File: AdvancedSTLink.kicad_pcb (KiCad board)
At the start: 2 copper layers, 61 x 19 mm, 50 parts, among them J1 USB_C_Receptacle, J2 Conn_02x03_Odd_Even, J3 Conn_01x06, SW1 SW_SPDT, U1 STM32F205RETx, U2 XC6206P332MR, U3 USBLC6-2P6, U4 MP2359, U5 USBLC6-2P6, U6 USBLC6-2P6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

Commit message: fabrication version
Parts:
- J3: value Conn_01x06 -> Conn_01x06_MountingPin
- moved J3 0.11 mm to (206.9, 106.4)
- moved D4 0.08 mm to (190.9, 113.0)
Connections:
- J3 pad MP: (no net) -> GND
- R1 pad 2: TCK1 -> RST1
- R6 pad 2: TCK2 -> RST2
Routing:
- net RST2: track 0.00 -> 41.2 mm, vias 0 -> 4
- net RST1: track 0.00 -> 37.2 mm, vias 0 -> 4
- net TCK1: track 59.6 -> 51.0 mm
- net TCK2: track 49.0 -> 41.8 mm, vias 4 -> 2
- net Net-(R2-Pad2): track 23.6 -> 21.7 mm, vias 2 -> 0
- net +3V3: track 111.9 -> 111.0 mm
- net GND: track 7.60 -> 7.08 mm, vias 62 -> 81
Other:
- board text added: "J8Link"
- board text removed: "STLink"

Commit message: Rev 2
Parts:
- removed R10, R11, R12, R13, R18, R6: 220, Resistor_SMD:R_0603_1608Metric
- added D6: LED_Blue, LED_SMD:LED_0603_1608Metric_Pad1.05x0.95mm_HandSolder, F.Cu at (161.3, 136.5)
- added D7: SS34, lc:SMA(DO-214AC)_S1, F.Cu at (154.1, 137.3)
- added J4: Conn_02x03_Odd_Even, Connector_PinHeader_1.27mm:PinHeader_2x03_P1.27mm_Vertical, F.Cu at (165.1, 128.5)
- added RN1: 220×4, lc:0402_RX4, F.Cu at (170.3, 128.4)
- added RN2: 220×4, lc:0402_RX4, F.Cu at (165.3, 134.3)
- C1, C2: value 10pF -> 12pF; footprint Capacitor_SMD:C_0603_1608Metric -> Capacitor_SMD:C_0402_1005Metric
- C10, C11, C13, C14, C3, C4, C5, C7, C8, C9: footprint Capacitor_SMD:C_0603_1608Metric -> Capacitor_SMD:C_0402_1005Metric
- D3: value B230A -> SS34; footprint Diode_SMD:D_SMA -> lc:SMA(DO-214AC)_S1
- D4: footprint Diode_SMD:D_SOD-123 -> lc:SOD-123
- J3: value Conn_01x06_MountingPin -> Conn_01x06
- R1: value 220 -> 39k; footprint Resistor_SMD:R_0603_1608Metric -> Resistor_SMD:R_0402_1005Metric
- R14, R15, R17, R2, R4, R5, R7, R8: footprint Resistor_SMD:R_0603_1608Metric -> Resistor_SMD:R_0402_1005Metric
- R16: value 1.5k -> 1.8k; footprint Resistor_SMD:R_0603_1608Metric -> Resistor_SMD:R_0402_1005Metric
- R9: value 330k -> 2.2k; footprint Resistor_SMD:R_0603_1608Metric -> Resistor_SMD:R_0402_1005Metric
- U1: moved to B.Cu
- U2: footprint Package_TO_SOT_SMD:SOT-23 -> lc:SOT-23-3L
- U4: footprint Package_TO_SOT_SMD:SOT-23-6 -> lc:SOT-23-6
- Y1: value DXS321G 8MHz -> NX3225GA-12MHz
- moved J3 56.3 mm to (156.5, 131.4), turned to 0 degrees
- moved R1 53.0 mm to (160.5, 138.8), turned to 0 degrees
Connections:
- C6 pad 1: VBUS -> Net-(C6-Pad1)
- J3 pad MP: GND -> (no net)
- R1 pad 2: RST1 -> Net-(D6-Pad2)
- R9 pad 1: VBUS -> +3V3
- SW1 pad 1: GND -> Net-(R9-Pad2)
- SW1 pad 2: Net-(R9-Pad2) -> Net-(D6-Pad2)
- SW1 pad 3: Net-(SW1-Pad3) -> GND
- U4 pad 4: Net-(R9-Pad2) -> Net-(R1-Pad1)
- U4 pad 5: VBUS -> Net-(C6-Pad1)
- U5 pad 4: Net-(R12-Pad2) -> T_SWO_I
- U5 pad 6: Net-(R1-Pad1) -> T_NRST_I
- U6 pad 4: Net-(R13-Pad2) -> T_SWDIO_I
- U6 pad 6: Net-(R10-Pad1) -> T_SWCLK_I
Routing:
- net +3V3: track 111.0 -> 0.00 mm, vias 10 -> 0
- net VBUS: track 57.8 -> 0.00 mm
- net TCK1: track 51.0 -> 0.00 mm
- net V_OUT_3.3: track 47.7 -> 0.00 mm, vias 4 -> 0
- net TDO: track 43.0 -> 0.00 mm, vias 2 -> 0
- net TCK2: track 41.8 -> 0.00 mm, vias 2 -> 0
- net RST2: track 41.2 -> 0.00 mm, vias 4 -> 0
- net RST1: track 37.2 -> 0.00 mm, vias 4 -> 0
- net TMS1: track 35.6 -> 0.00 mm
- net TMS2: track 35.4 -> 0.00 mm
- net LED1: track 32.0 -> 0.00 mm, vias 2 -> 0
- net LED2: track 29.0 -> 0.00 mm, vias 2 -> 0
- net Net-(R2-Pad2): track 21.7 -> 0.00 mm
- net STM_NRST: track 21.0 -> 0.00 mm, vias 1 -> 0
- net Net-(R9-Pad2): track 18.9 -> 0.00 mm, vias 2 -> 0
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
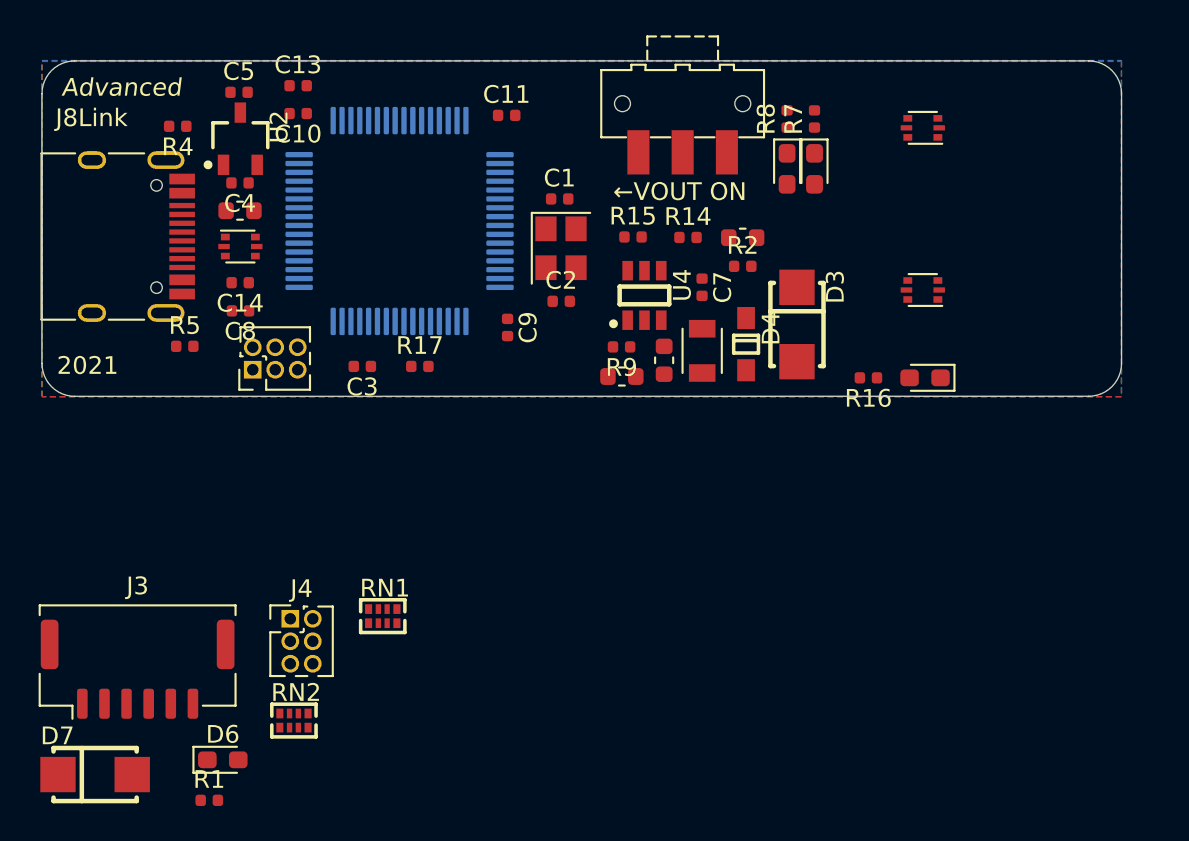
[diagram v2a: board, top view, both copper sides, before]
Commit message: Put components.
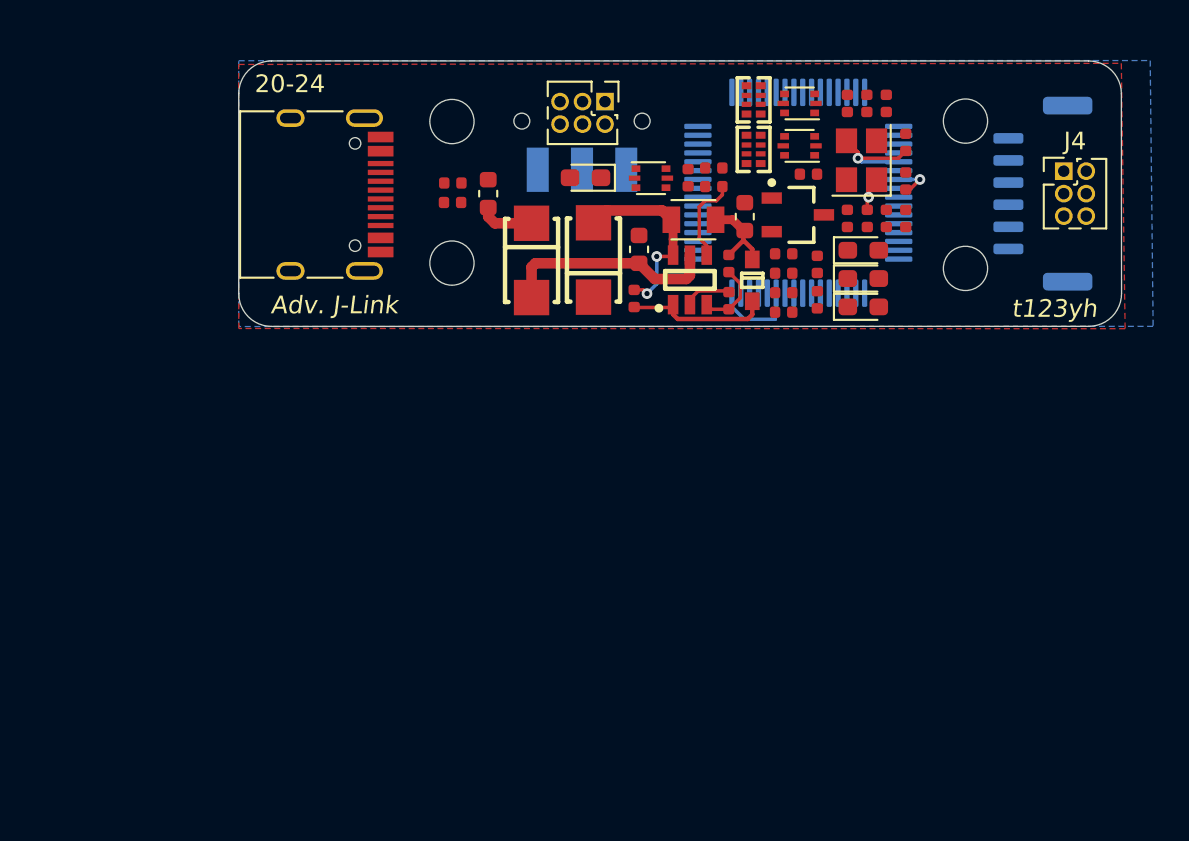
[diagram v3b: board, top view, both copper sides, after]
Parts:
- added H1: MountingHole, MountingHole:MountingHole_2.5mm, F.Cu at (203.3, 100.4)
- added H2: MountingHole, MountingHole:MountingHole_2.5mm, F.Cu at (203.3, 108.7)
- added H3: MountingHole, MountingHole:MountingHole_2.5mm, F.Cu at (174.2, 100.4)
- added H4: MountingHole, MountingHole:MountingHole_2.5mm, F.Cu at (174.2, 108.4)
- C1, C2: value 12pF -> 33pF
- D4: footprint lc:SOD-123 -> lc:SOD-323
- J3, SW1: moved to B.Cu
- R3: footprint Resistor_SMD:R_0603_1608Metric -> Resistor_SMD:R_0402_1005Metric
- Y1: value NX3225GA-12MHz -> X322512MSB4SI
- moved J3 57.8 mm to (207.7, 104.5), turned to 90 degrees
- moved J4 50.5 mm to (208.8, 103.2)
- moved R1 44.9 mm to (189.1, 104.1), turned to 180 degrees
- moved RN2 43.7 mm to (191.3, 99.2), turned to 90 degrees
- moved D6 38.8 mm to (181.8, 103.6), turned to 180 degrees
- moved C8 38.3 mm to (198.8, 99.4), turned to 90 degrees
- moved D7 38.1 mm to (178.8, 108.3), turned to 270 degrees
- moved C5 34.1 mm to (194.9, 108.5), turned to 270 degrees
- moved RN1 33.7 mm to (191.3, 102.0), turned to 90 degrees
- moved C3 32.5 mm to (199.9, 103.8), turned to 270 degrees
- moved C4 32.1 mm to (194.4, 103.4)
- moved U2 31.8 mm to (193.8, 105.7), turned to 180 degrees
- moved C10 31.6 mm to (196.6, 105.9), turned to 90 degrees
- moved C13 30.3 mm to (193.0, 111.2), turned to 180 degrees
- moved R17 29.3 mm to (197.7, 99.4), turned to 90 degrees
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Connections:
- D5 pad 1: GND -> Net-(D5-Pad1)
- D5 pad 2: Net-(D5-Pad2) -> V_OUT_3.3
- R16 pad 1: Net-(D5-Pad2) -> GND
- R16 pad 2: V_OUT_3.3 -> Net-(D5-Pad1)
- U3 pad 5: VBUS -> Net-(FB1-Pad2)
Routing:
- net Net-(C6-Pad1): track 0.00 -> 12.4 mm
- net Net-(C7-Pad2): track 0.00 -> 11.0 mm, vias 0 -> 2
- net Net-(C7-Pad1): track 0.00 -> 8.27 mm
- net Net-(C2-Pad2): track 0.00 -> 6.51 mm, vias 0 -> 1
- net Net-(R1-Pad1): track 0.00 -> 4.96 mm
- net V_OUT_3.3: track 0.00 -> 4.84 mm
- net Net-(C1-Pad1): track 0.00 -> 4.58 mm, vias 0 -> 1
- net Net-(R14-Pad1): track 0.00 -> 4.00 mm
- net +3V3: track 0.00 -> 3.63 mm
- net VBUS: track 0.00 -> 3.12 mm
- net GND: track 0.00 -> 2.73 mm
- net STM_NRST: track 0.00 -> 2.24 mm, vias 0 -> 1
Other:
- board size 61 x 19 mm -> 49.9 x 15 mm
- board text added: "20-24"
- board text added: "Adv. J-Link"
- board text added: "t123yh"
- board text removed: "2021"
- board text removed: "Advanced"
- board text removed: "J8Link"
- board text removed: "←VOUT ON"

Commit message: Layout.
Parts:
- moved C9 8.89 mm to (188.1, 102.0), turned to 0 degrees
- moved R16 5.20 mm to (200.1, 110.6), turned to 90 degrees
- moved C14 4.73 mm to (188.1, 98.9), turned to 90 degrees
- moved R7 3.04 mm to (195.1, 110.1)
- moved R8 2.10 mm to (195.1, 109.0)
- moved C5 1.99 mm to (193.0, 107.9), turned to 0 degrees
- moved C8 1.50 mm to (197.3, 99.4), turned to 270 degrees
- moved R17 1.50 mm to (196.2, 99.4), turned to 270 degrees
- moved C11 1.10 mm to (193.1, 111.2)
- moved C13 1.10 mm to (193.1, 110.1)
- moved R2 1.10 mm to (198.8, 105.9), turned to 90 degrees
- moved R3 1.10 mm to (199.9, 105.9), turned to 90 degrees
- moved C6 0.37 mm to (184.7, 108.0)
- moved U4 0.32 mm to (187.4, 109.5)
- moved R15 0.30 mm to (189.6, 110.5)
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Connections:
- D5 pad 1: Net-(D5-Pad1) -> GND
- D5 pad 2: V_OUT_3.3 -> Net-(D5-Pad2)
- R16 pad 1: GND -> Net-(D5-Pad2)
- R16 pad 2: Net-(D5-Pad1) -> V_OUT_3.3
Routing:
- net +3V3: track 3.63 -> 72.9 mm, vias 0 -> 8
- net GND: track 2.73 -> 40.9 mm, vias 0 -> 14
- net V_OUT_3.3: track 4.84 -> 41.5 mm, vias 0 -> 2
- net T_SWCLK_O: track 0.00 -> 30.2 mm, vias 0 -> 1
- net T_SWDIO_O: track 0.00 -> 29.5 mm, vias 0 -> 1
- net Net-(FB1-Pad2): track 0.00 -> 29.3 mm, vias 0 -> 4
- net VBUS: track 3.12 -> 31.3 mm, vias 0 -> 2
- net STM_NRST: track 2.24 -> 27.2 mm, vias 1 -> 2
- net T_NRST_O: track 0.00 -> 24.9 mm, vias 0 -> 2
- net T_SWO_O: track 0.00 -> 23.9 mm, vias 0 -> 2
- net USB_IN_DP: track 0.00 -> 18.3 mm, vias 0 -> 2
- net TCK1: track 0.00 -> 18.1 mm, vias 0 -> 1
- net USB_IN_DN: track 0.07 -> 17.3 mm, vias 0 -> 2
- net TDO: track 0.00 -> 16.2 mm, vias 0 -> 2
- net TMS1: track 0.00 -> 15.4 mm, vias 0 -> 2
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- added copper zone on In2.Cu, net GND
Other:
- copper layers 2 -> 4
- net class Default: clearance 0.127 -> 0.15
- rule trace_clearance: 0.127 -> 0.15

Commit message: DRC fixes
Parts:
- added C15: 100nF, Capacitor_SMD:C_0402_1005Metric, F.Cu at (203.5, 104.5)
- moved D6 0.36 mm to (181.5, 103.4)
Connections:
- J3 pad MP: (no net) -> GND
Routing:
- net GND: track 40.9 -> 53.6 mm, vias 14 -> 30
- net V_OUT_3.3: track 41.5 -> 43.7 mm, vias 2 -> 3
- net TDO: track 16.2 -> 17.8 mm
- net Net-(D6-Pad2): track 10.6 -> 12.0 mm
- net +3V3: track 72.9 -> 74.2 mm
- net Net-(C7-Pad1): track 8.40 -> 9.01 mm
- net (no net): vias 2 -> 0

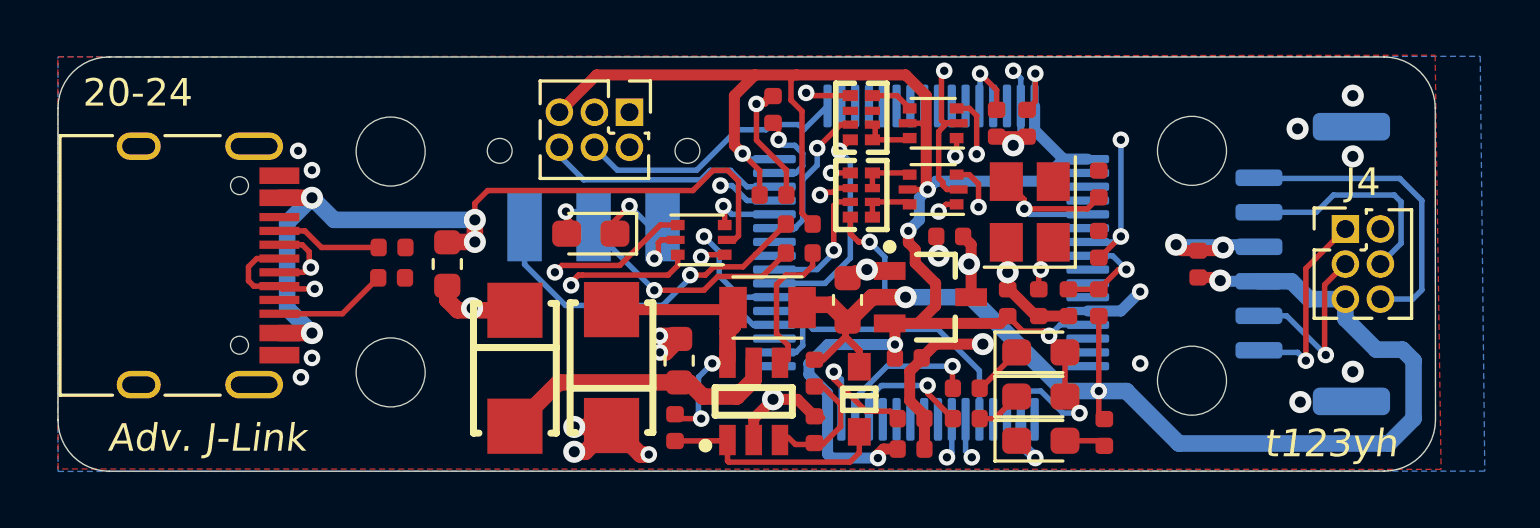
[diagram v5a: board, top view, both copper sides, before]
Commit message: Enhance grounding.
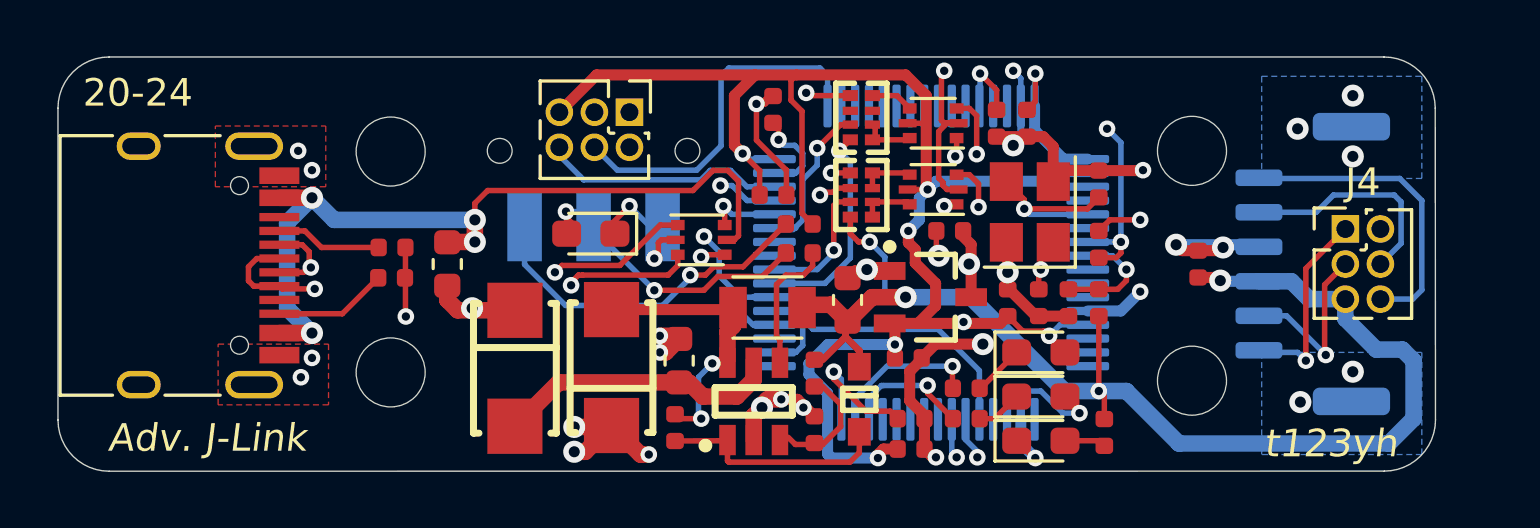
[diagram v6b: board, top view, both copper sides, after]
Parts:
- moved C4 0.20 mm to (194.5, 103.3)
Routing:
- net GND: track 53.6 -> 64.3 mm, vias 30 -> 35
- net +3V3: track 74.2 -> 78.6 mm, vias 8 -> 9
- net STM_SWCLK: track 9.91 -> 13.0 mm
- net TMS2: track 14.3 -> 14.8 mm

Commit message: Add teardrops.
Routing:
- net GND: track 64.3 -> 65.7 mm, vias 35 -> 36
